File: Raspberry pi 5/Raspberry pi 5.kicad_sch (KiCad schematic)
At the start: 6 parts, among them J1 GPIO, U1 CAT24C256

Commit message: 新增了type-c port
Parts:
- added J2: USB4105-GF-A, USB4105-GF-A:GCT_USB4105-GF-A, symbol USB4105-GF-A:USB4105-GF-A
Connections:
- net GND: now also J2.A1_B12 (GND), J2.B1_A12 (GND)
- new net SHELL_GND: J2.SH1 (SHELL_GND), J2.SH2 (SHELL_GND), J2.SH3 (SHELL_GND), J2.SH4 (SHELL_GND)
- new net VBUS: J2.A4_B9 (VBUS), J2.B4_A9 (VBUS)

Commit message: 新修正了type-c port info
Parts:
- J2: MPN (none) -> USB4105-GF-A
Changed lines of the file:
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@@
+			)
+		)
+		(property "MPN" "USB4105-GF-A"
+			(at 194.31 54.61 0)
+			(hide yes)
+			(show_name no)
+			(do_not_autoplace no)
+			(effects
+				(font
+					(size 1.27 1.27)
+				)
 			)
 		)

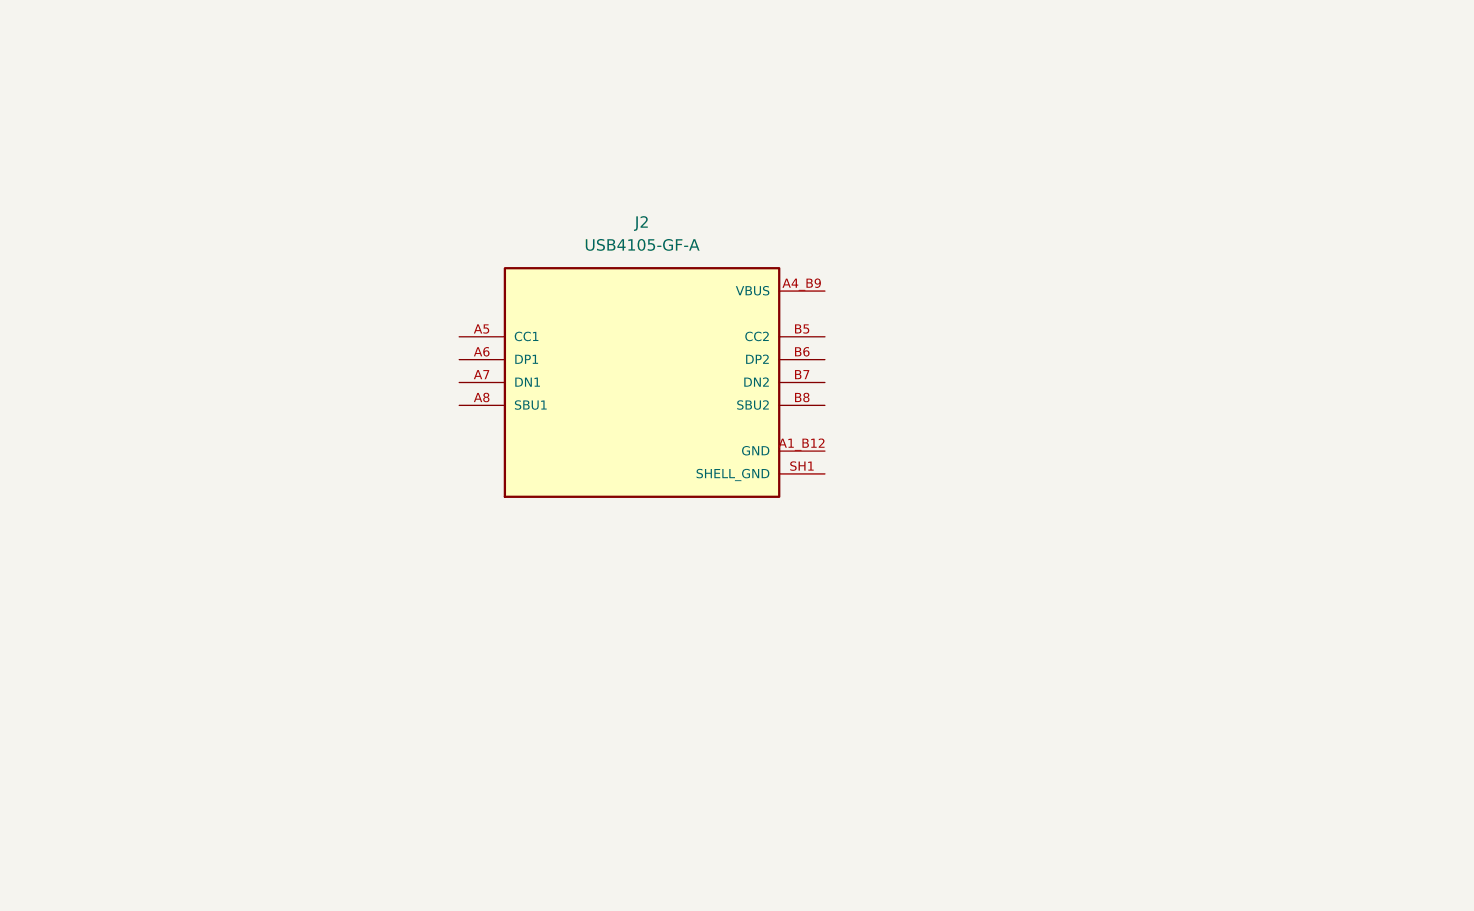
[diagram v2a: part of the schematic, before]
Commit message: update the pi 5
add the pi 5 components
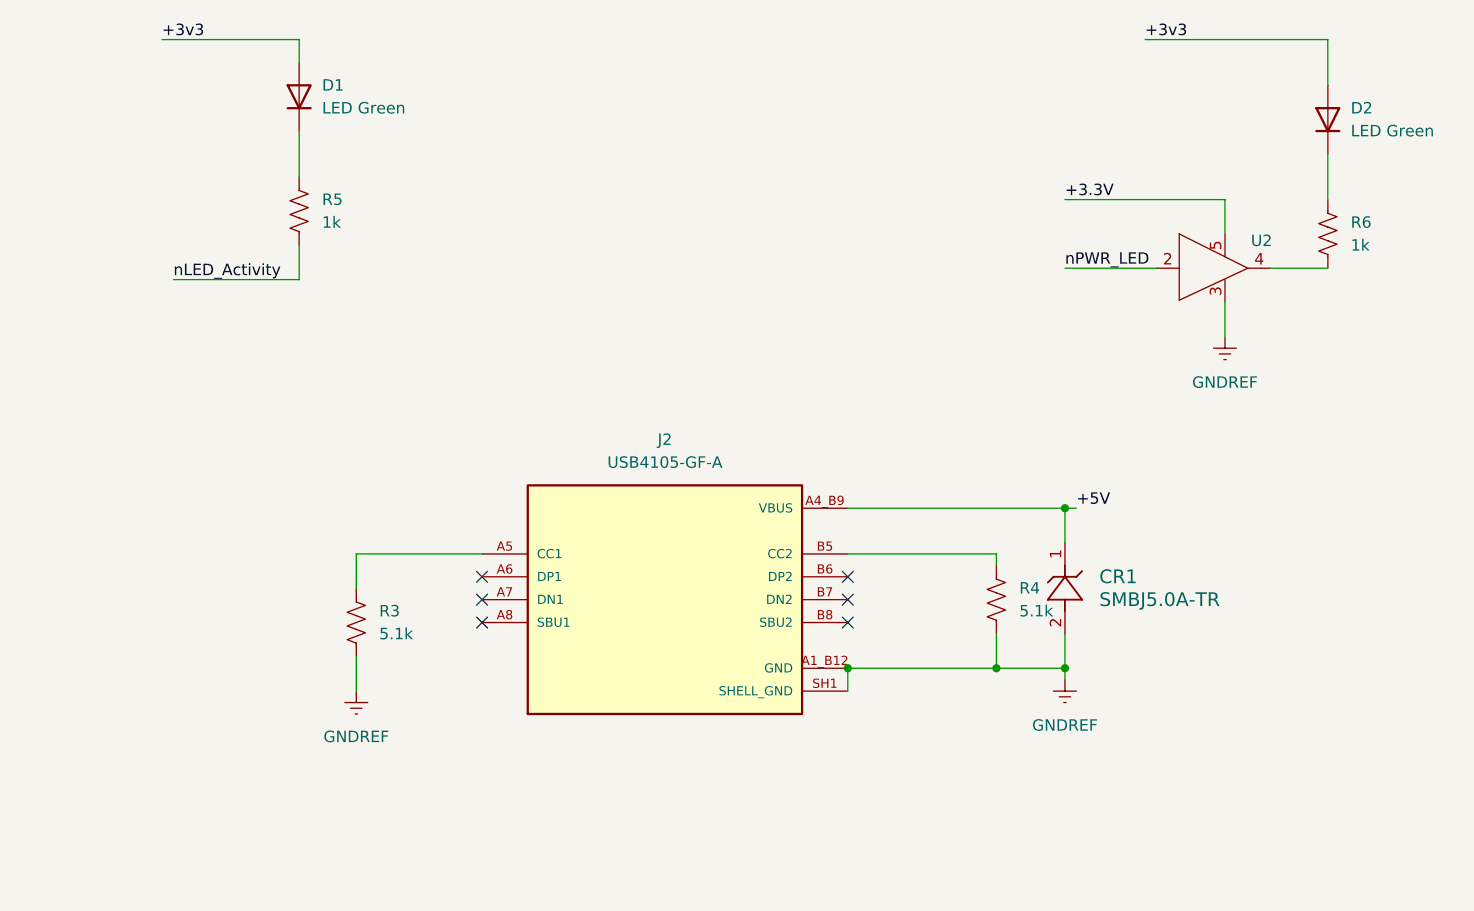
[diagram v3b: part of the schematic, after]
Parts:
- added CR1: SMBJ5.0A-TR, SMB_STM, symbol 2026-07-23_02-52-56:SMBJ5.0A-TR
- added D1, D2: LED Green, symbol Device:D
- added R3, R4: 5.1k, symbol Device:R_US
- added R5, R6: 1k, symbol Device:R_US
- added U2: (no value), symbol 74LVC1G07SE-7:74LVC1G07SE-7
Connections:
- net SHELL_GND is gone; now on net GND: J2.SH1 (SHELL_GND), J2.SH2 (SHELL_GND), J2.SH3 (SHELL_GND), J2.SH4 (SHELL_GND)
- net VBUS is gone; now on net +5V: J2.A4_B9 (VBUS), J2.B4_A9 (VBUS)
- net +5V: now also CR1.1
- net GND: now also CR1.2, R3.2, R4.2, U2.3
- net at J2.A5 (CC1): now also R3.1
- net at J2.B5 (CC2): now also R4.1
- new net: D2.1 (K), R6.1
- new net: D1.1 (K), R5.1
- new net: R6.2, U2.4
- new net +3.3V: U2.5
- new net +3v3: D1.2 (A), D2.2 (A)
- new net nLED_Activity: R5.2
- new net nPWR_LED: U2.2
- no-connect marks 3 -> 9
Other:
- moved on the sheet: J2

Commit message: 新增 2x DF40C-100DS-0.4V components
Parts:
- removed CR1: SMBJ5.0A-TR, SMB_STM, symbol 2026-07-23_02-52-56:SMBJ5.0A-TR
- removed D1, D2: LED Green, symbol Device:D
- removed J2: USB4105-GF-A, USB4105-GF-A:GCT_USB4105-GF-A, symbol USB4105-GF-A:USB4105-GF-A
- removed R3, R4: 5.1k, symbol Device:R_US
- removed R5, R6: 1k, symbol Device:R_US
- removed U2: (no value), symbol 74LVC1G07SE-7:74LVC1G07SE-7
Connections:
- no-connect marks 9 -> 3
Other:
- added sheet ComputeModule4 (ComputeModule4.kicad_sch)

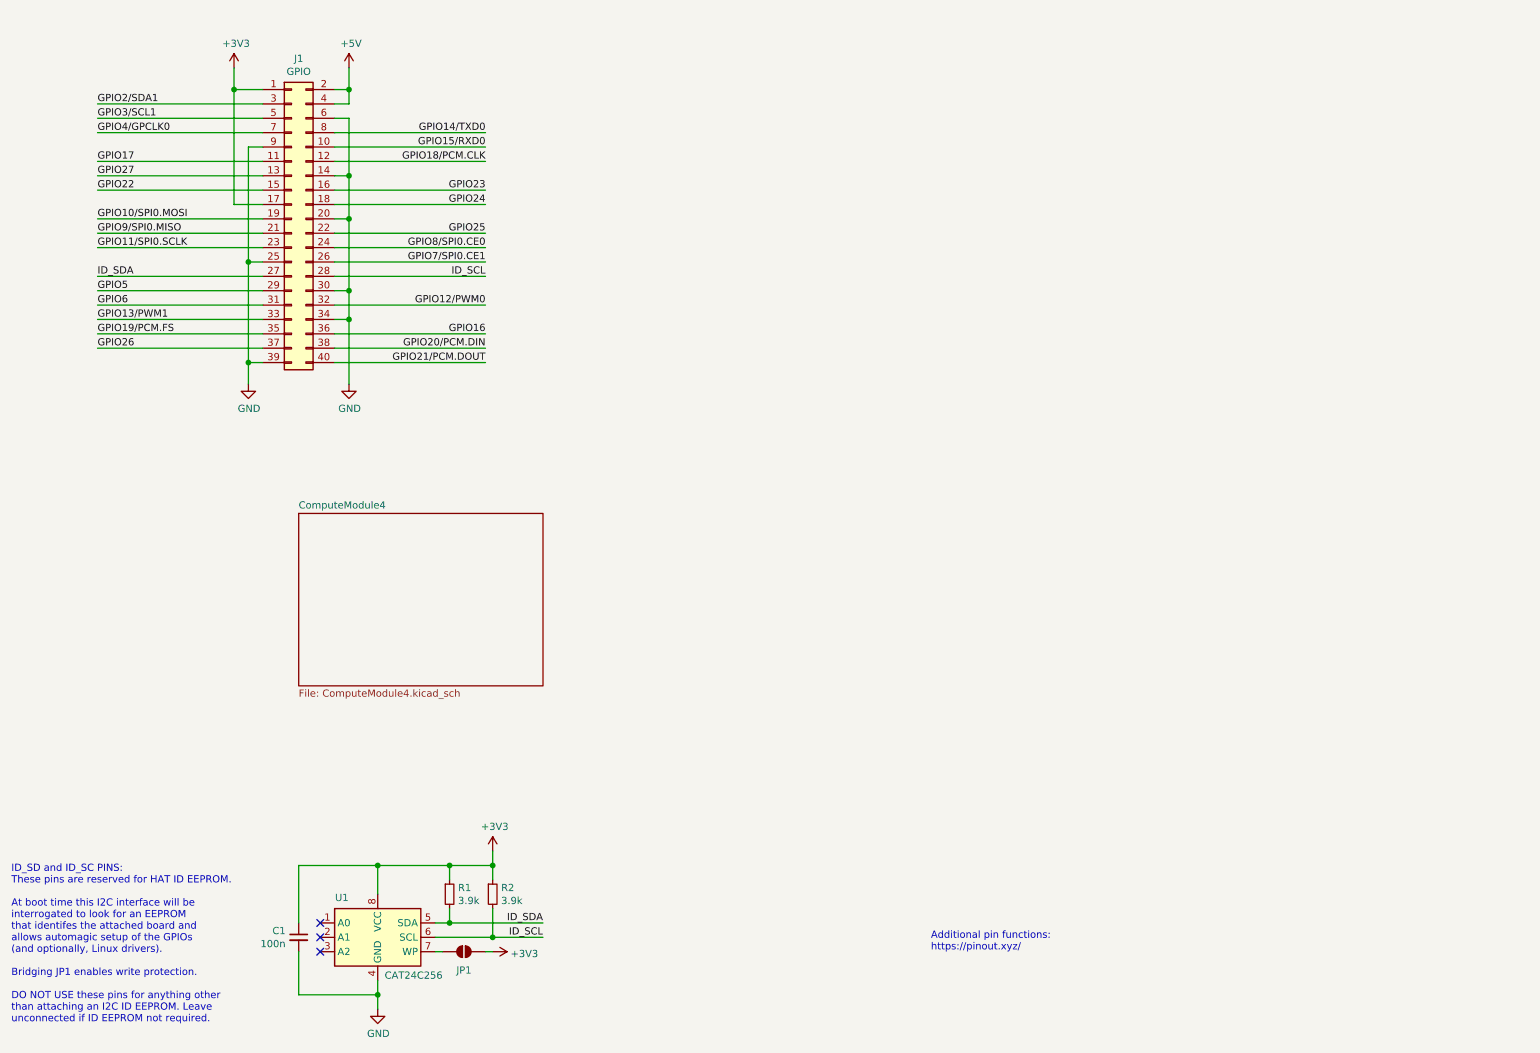
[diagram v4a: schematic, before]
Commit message: add CM4 Ethernet and High Speed
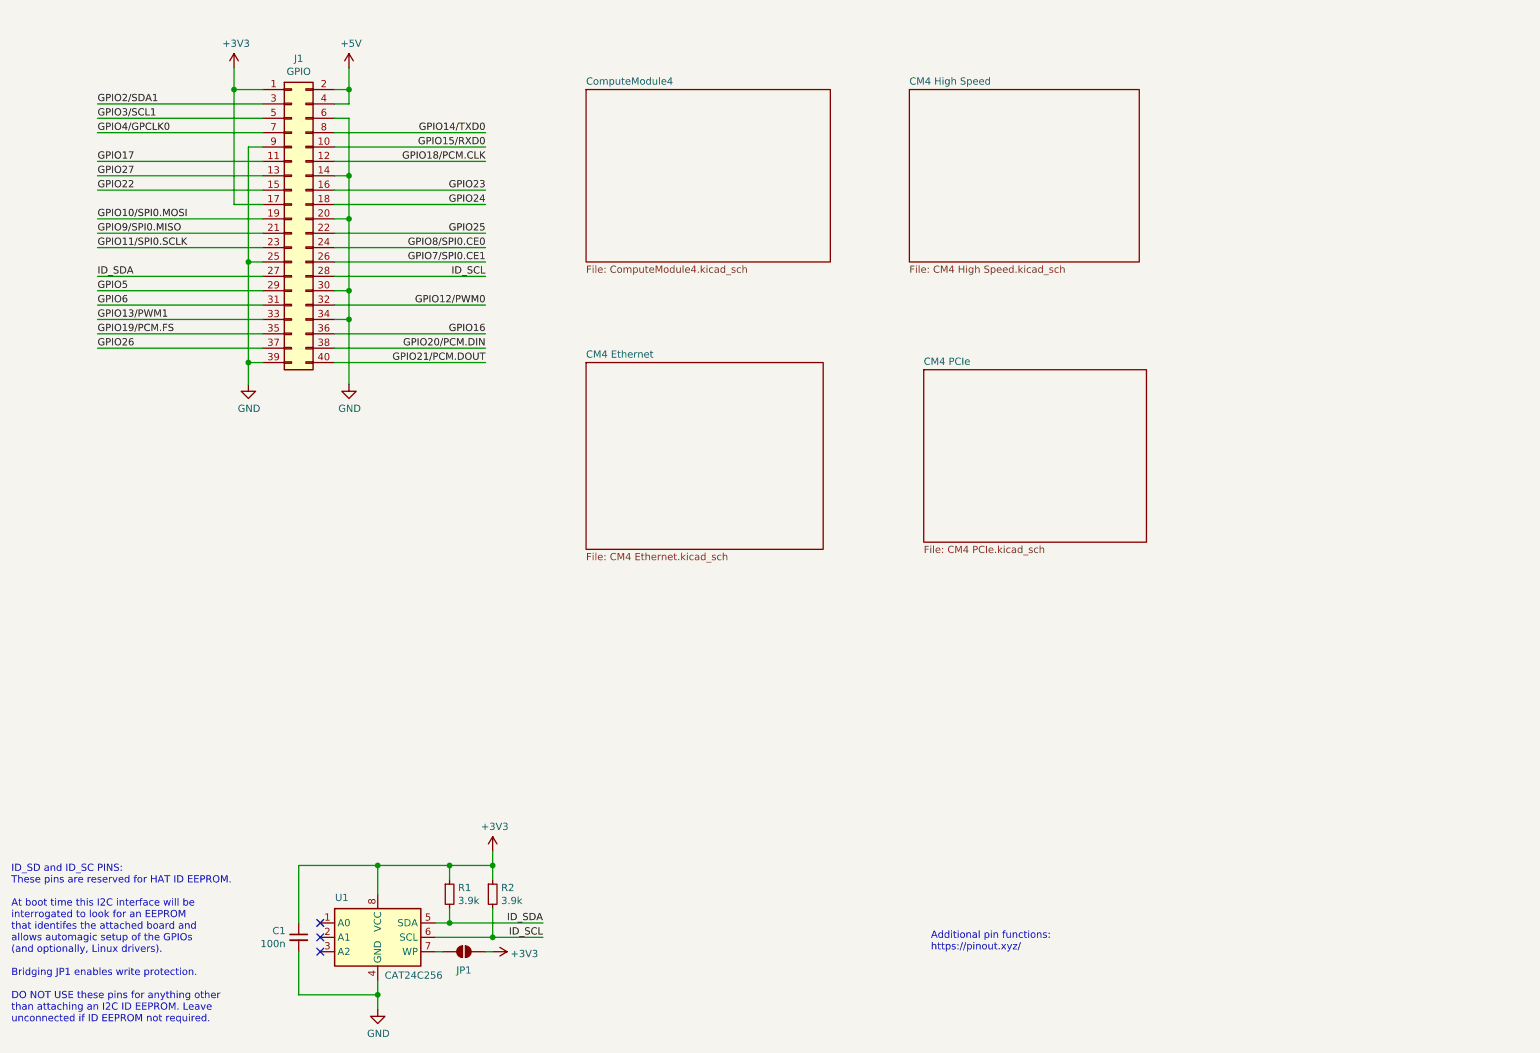
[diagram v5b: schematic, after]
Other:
- added sheet CM4 Ethernet (CM4 Ethernet.kicad_sch)
- added sheet CM4 High Speed (CM4 High Speed.kicad_sch)
- added sheet CM4 PCIe (CM4 PCIe.kicad_sch)
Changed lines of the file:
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@@
 	)
 	(sheet
-		(at 67.31 102.87)
+		(at 175.26 27.94)
+		(size 40.64 30.48)
+		(exclude_from_sim no)
+		(in_bom yes)
+		(on_board yes)
+		(dnp no)
+		(fields_autoplaced yes)
+		(stroke
+			(width 0.1524)
+			(type solid)
+		)
+		(fill
+			(color 0 0 0 0)
+		)
+		(property "Sheetname" "CM4 High Speed"
+			(at 175.26 27.2284 0)
+			(show_name no)
+			(do_not_autoplace no)
+			(effects
+				(font
+					(size 1.27 1.27)
+				)
+				(justify left bottom)
+			)
+		)
+		(property "Sheetfile" "CM4 High Speed.kicad_sch"
+			(at 175.26 59.0046 0)
+			(show_name no)
+			(do_not_autoplace no)
+			(effects
+				(font
+					(size 1.27 1.27)
+				)
+				(justify left top)
+			)
+		)
+		(instances
+			(project "Raspberry pi 5"
+				(path "/e63e39d7-6ac0-4ffd-8aa3-1841a4541b55"
+					(page "3")
+				)
+			)
+		)
+	)
+	(sheet
+		(at 177.8 77.47)
+		(size 39.37 30.48)
+		(exclude_from_sim no)
+		(in_bom yes)
+		(on_board yes)
+		(dnp no)
+		(fields_autoplaced yes)
+		(stroke
+			(width 0.1524)
+			(type solid)
+		)
+		(fill
+			(color 0 0 0 0)
+		)
+		(property "Sheetname" "CM4 PCIe"
+			(at 177.8 76.7584 0)
+			(show_name no)
+			(do_not_autoplace no)
+			(effects
+				(font
+					(size 1.27 1.27)
+				)
+				(justify left bottom)
+			)
+		)
+		(property "Sheetfile" "CM4 PCIe.kicad_sch"
+			(at 177.8 108.5346 0)
+			(show_name no)
+			(do_not_autoplace no)
+			(effects
+				(font
+					(size 1.27 1.27)
+				)
+				(justify left top)
+			)
+		)
+		(instances
+			(project "Raspberry pi 5"
+				(path "/e63e39d7-6ac0-4ffd-8aa3-1841a4541b55"
+					(page "5")
+				)
+			)
+		)
+	)
+	(sheet
+		(at 118.11 76.2)
+		(size 41.91 33.02)
+		(exclude_from_sim no)
+		(in_bom yes)
+		(on_board yes)
+		(dnp no)
+		(fields_autoplaced yes)
+		(stroke
+			(width 0.1524)
+			(type solid)
+		)
+		(fill
+			(color 0 0 0 0)
+		)
+		(property "Sheetname" "CM4 Ethernet"
+			(at 118.11 75.4884 0)
+			(show_name no)
+			(do_not_autoplace no)
+			(effects
+				(font
+					(size 1.27 1.27)
+				)
+				(justify left bottom)
+			)
+		)
+		(property "Sheetfile" "CM4 Ethernet.kicad_sch"
+			(at 118.11 109.8046 0)
+			(show_name no)
+			(do_not_autoplace no)
+			(effects
+				(font
+					(size 1.27 1.27)
+				)
+				(justify left top)
+			)
+		)
+		(instances
+			(project "Raspberry pi 5"
+				(path "/e63e39d7-6ac0-4ffd-8aa3-1841a4541b55"
+					(page "4")
+				)
+			)
+		)
+	)
+	(sheet
+		(at 118.11 27.94)
 		(size 43.18 30.48)
 		(exclude_from_sim no)
@@
 		)
 		(property "Sheetname" "ComputeModule4"
-			(at 67.31 102.1584 0)
+			(at 118.11 27.2284 0)
 			(show_name no)
 			(do_not_autoplace no)
@@
 		)
 		(property "Sheetfile" "ComputeModule4.kicad_sch"
-			(at 67.31 133.9346 0)
+			(at 118.11 59.0046 0)
 			(show_name no)
 			(do_not_autoplace no)

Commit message: 繪製CM4 Enternet
進度達1/3
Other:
- added sheet CM4 USB (CM4 USB.kicad_sch)
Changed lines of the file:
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@@
+		)
+	)
+	(sheet
+		(at 118.11 121.92)
+		(size 41.91 33.02)
+		(exclude_from_sim no)
+		(in_bom yes)
+		(on_board yes)
+		(dnp no)
+		(fields_autoplaced yes)
+		(stroke
+			(width 0.1524)
+			(type solid)
+		)
+		(fill
+			(color 0 0 0 0)
+		)
+		(property "Sheetname" "CM4 USB"
+			(at 118.11 121.2084 0)
+			(show_name no)
+			(do_not_autoplace no)
+			(effects
+				(font
+					(size 1.27 1.27)
+				)
+				(justify left bottom)
+			)
+		)
+		(property "Sheetfile" "CM4 USB.kicad_sch"
+			(at 118.11 155.5246 0)
+			(show_name no)
+			(do_not_autoplace no)
+			(effects
+				(font
+					(size 1.27 1.27)
+				)
+				(justify left top)
+			)
+		)
+		(instances
+			(project "Raspberry pi 5"
+				(path "/e63e39d7-6ac0-4ffd-8aa3-1841a4541b55"
+					(page "6")
+				)
+			)
 		)
 	)

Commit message: update the cm4 USB port
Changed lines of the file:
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@@
 	)
 	(sheet
-		(at 175.26 27.94)
-		(size 40.64 30.48)
+		(at 163.83 49.53)
+		(size 43.18 29.21)
 		(exclude_from_sim no)
 		(in_bom yes)
@@
 		)
 		(property "Sheetname" "CM4 High Speed"
-			(at 175.26 27.2284 0)
+			(at 163.83 48.8184 0)
 			(show_name no)
 			(do_not_autoplace no)
@@
 		)
 		(property "Sheetfile" "CM4 High Speed.kicad_sch"
-			(at 175.26 59.0046 0)
+			(at 163.83 79.3246 0)
 			(show_name no)
 			(do_not_autoplace no)
@@
 	)
 	(sheet
-		(at 177.8 77.47)
-		(size 39.37 30.48)
+		(at 162.56 88.9)
+		(size 43.18 33.02)
 		(exclude_from_sim no)
 		(in_bom yes)
@@
 		)
 		(property "Sheetname" "CM4 PCIe"
-			(at 177.8 76.7584 0)
+			(at 162.56 88.1884 0)
 			(show_name no)
 			(do_not_autoplace no)
@@
 		)
 		(property "Sheetfile" "CM4 PCIe.kicad_sch"
-			(at 177.8 108.5346 0)
+			(at 162.56 122.5046 0)
 			(show_name no)
 			(do_not_autoplace no)
@@
 	)
 	(sheet
-		(at 118.11 76.2)
+		(at 118.11 88.9)
 		(size 41.91 33.02)
 		(exclude_from_sim no)
@@
 		)
 		(property "Sheetname" "CM4 Ethernet"
-			(at 118.11 75.4884 0)
+			(at 118.11 88.1884 0)
 			(show_name no)
 			(do_not_autoplace no)
@@
 		)
 		(property "Sheetfile" "CM4 Ethernet.kicad_sch"
-			(at 118.11 109.8046 0)
+			(at 118.11 122.5046 0)
 			(show_name no)
 			(do_not_autoplace no)
@@
 	)
 	(sheet
-		(at 118.11 27.94)
+		(at 118.11 49.53)
 		(size 43.18 30.48)
 		(exclude_from_sim no)
@@
 		)
 		(property "Sheetname" "ComputeModule4"
-			(at 118.11 27.2284 0)
+			(at 118.11 48.8184 0)
 			(show_name no)
 			(do_not_autoplace no)
@@
 		)
 		(property "Sheetfile" "ComputeModule4.kicad_sch"
-			(at 118.11 59.0046 0)
+			(at 118.11 80.5946 0)
 			(show_name no)
 			(do_not_autoplace no)
@@
 	)
 	(sheet
-		(at 118.11 121.92)
-		(size 41.91 33.02)
+		(at 119.38 130.81)
+		(size 40.64 31.75)
 		(exclude_from_sim no)
 		(in_bom yes)
@@
 		)
 		(property "Sheetname" "CM4 USB"
-			(at 118.11 121.2084 0)
+			(at 119.38 130.0984 0)
 			(show_name no)
 			(do_not_autoplace no)
@@
 		)
 		(property "Sheetfile" "CM4 USB.kicad_sch"
-			(at 118.11 155.5246 0)
-			(show_name no)
-			(do_not_autoplace no)
+			(at 119.38 163.1446 0)
+			(show_name no)
+			(do_not_autoplace no)
